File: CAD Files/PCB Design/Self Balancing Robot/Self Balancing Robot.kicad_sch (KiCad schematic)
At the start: 9 parts, among them M1 Stepper_Motor_bipolar, M2 Stepper_Motor_bipolar, U1 DEVKIT_V1_ESP32-WROOM-32, U2 TSR_1-2450

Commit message: Added battery terminal, updated capacitor symbol, and assigned footprints.
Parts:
- removed C1, C2: 100 μF, symbol Device:C
- removed U1: DEVKIT_V1_ESP32-WROOM-32, DEVKIT_V1_ESP32-WROOM-32:MODULE_DEVKIT_V1_ESP32-WROOM-32, symbol DEVKIT_V1_ESP32-WROOM-32:DEVKIT_V1_ESP32-WROOM-32
- added C1, C2: ECA1HM101, TW Footprints:CAPPRD350W60D800H1150, symbol TW_Symbols:ECA1HM101
- added J1: Screw_Terminal_01x02, TerminalBlock:TerminalBlock_MaiXu_MX126-5.0-02P_1x02_P5.00mm, symbol Connector:Screw_Terminal_01x02
- added U1: DEVKIT_V1_ESP32-WROOM-32, TW Footprints:MODULE_DEVKIT_V1_ESP32-WROOM-32, symbol TW_Symbols:DEVKIT_V1_ESP32-WROOM-32
- M1, M2: footprint (none) -> Connector_JST:JST_XH_B4B-XH-A_1x04_P2.50mm_Vertical
- MPU1: footprint (none) -> Connector_PinHeader_1.00mm:PinHeader_1x08_P1.00mm_Vertical
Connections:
- net +12V: now also C1.P, C2.P, J1.1 (Pin_1)
- net Direc1: now also U1.10 (D19)
- net Direc2: now also U1.24 (D26)
- net GND: now also C1.N, C2.N, J1.2 (Pin_2), U1.2 (GND), U1.29 (GND)
- net SCL: now also U1.14 (D22)
- net SDA: now also U1.11 (D21)
- net Step1: now also U1.9 (D18)
- net Step2: now also U1.23 (D25)
- net VDD: now also A2.13 (~{RESET}), A2.14 (~{SLEEP}), U1.30 (VIN)

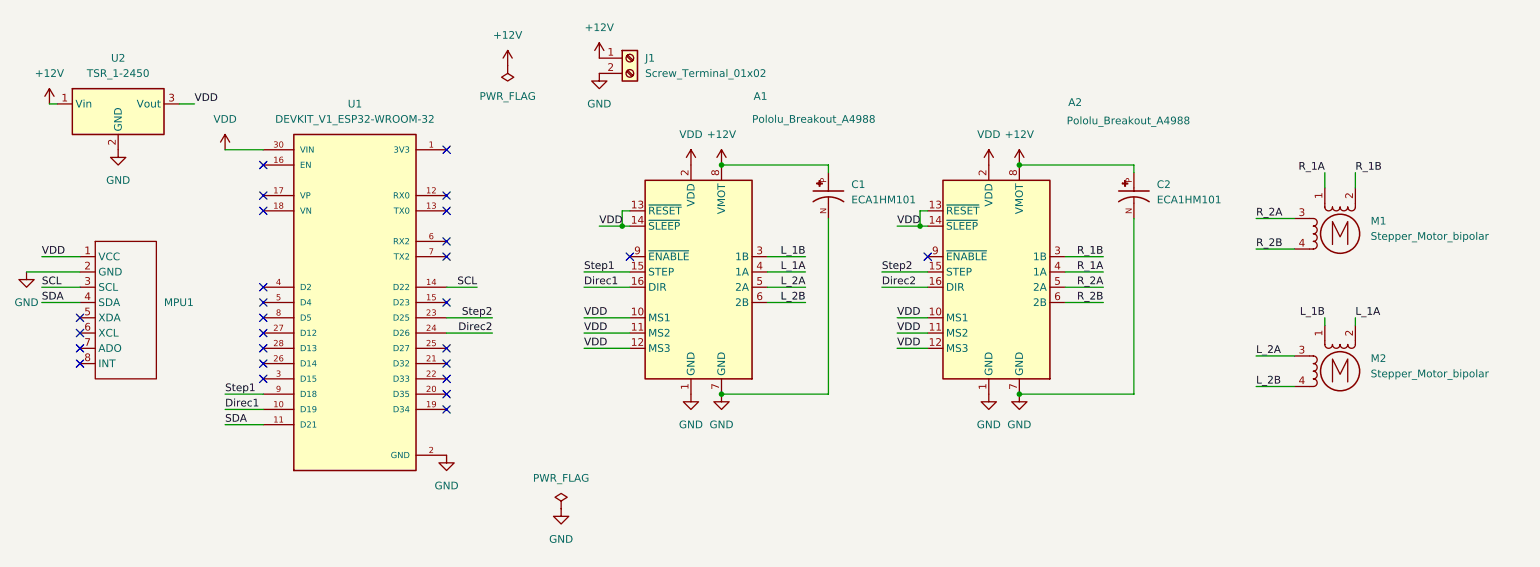
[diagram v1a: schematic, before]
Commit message: Fix schematic by adding screw terminal for battery, added indicator LEDS (and resistors), made custom footprints for capacitors, LEDS, configured libraries, made gitignore for PCB design folder
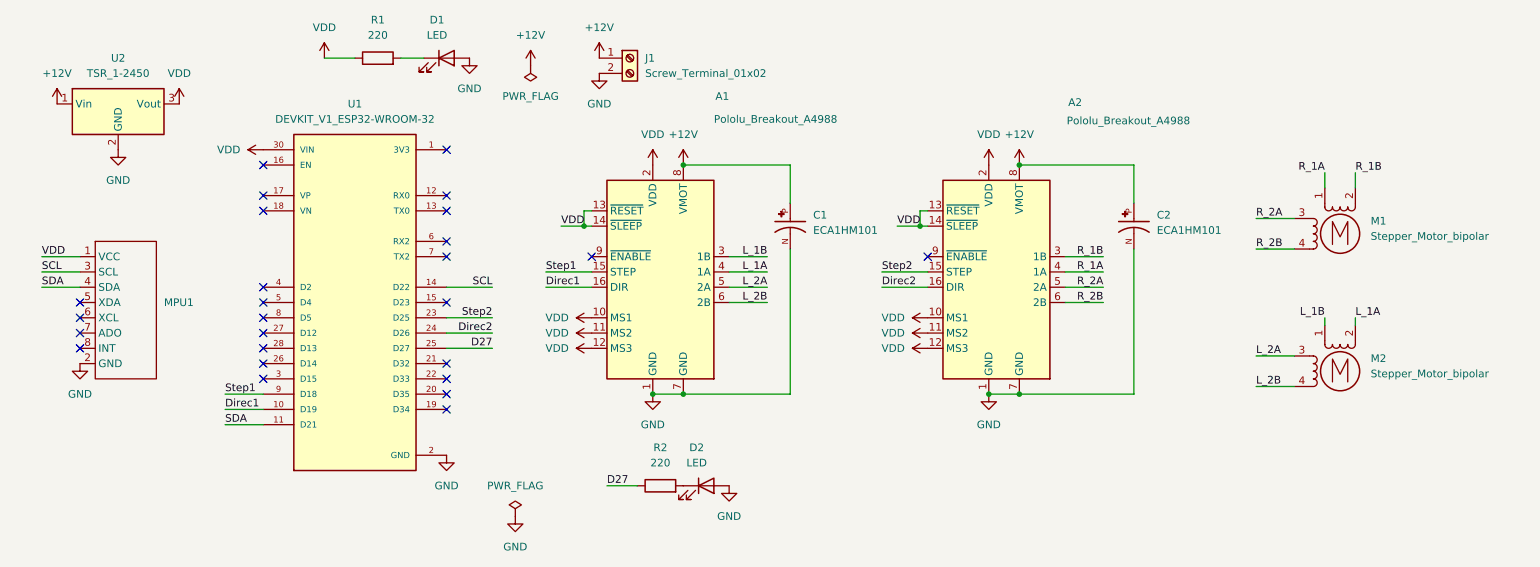
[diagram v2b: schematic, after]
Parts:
- added D1, D2: LED, TW Footprints:SMD LED 1206, symbol Device:LED
- added R1, R2: 220, Resistor_SMD:R_1206_3216Metric_Pad1.30x1.75mm_HandSolder, symbol Device:R
- C1, C2: footprint TW Footprints:CAPPRD350W60D800H1150 -> TW Footprints:CP_Radial_D6.3mm_P2.50mm
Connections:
- net GND: now also D1.2 (A), D2.2 (A)
- net VDD: now also R1.1
- net D27: now reaches U1.25 (D27)
- net D27: now also R2.1
- new net: D2.1 (K), R2.2
- new net: D1.1 (K), R1.2
- no-connect marks 27 -> 26
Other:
- moved on the sheet: A1, C1, C2

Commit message: Added MPU (GY-521) footprint
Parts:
- MPU1: footprint Connector_PinHeader_1.00mm:PinHeader_1x08_P1.00mm_Vertical -> TW Footprints:MODULE_GY-521
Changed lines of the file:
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@@
 			)
 		)
-		(property "Footprint" "Connector_PinHeader_1.00mm:PinHeader_1x08_P1.00mm_Vertical"
+		(property "Footprint" "TW Footprints:MODULE_GY-521"
 			(at 44.45 58.42 0)
 			(effects

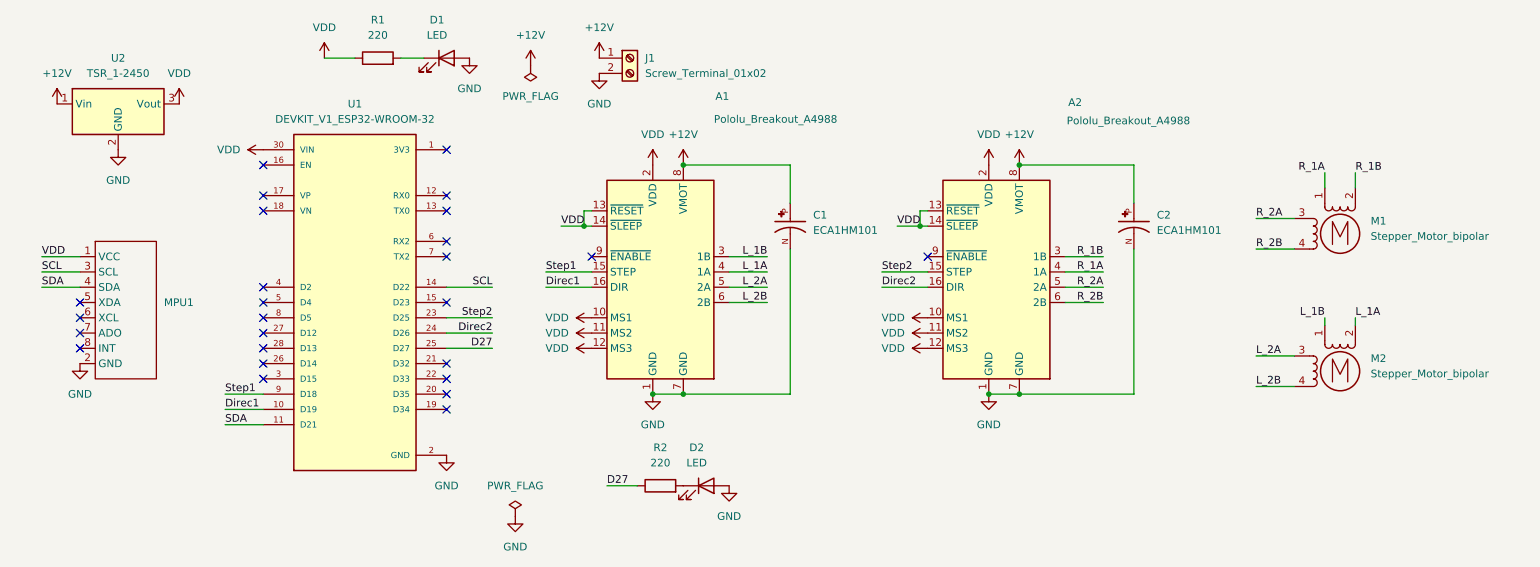
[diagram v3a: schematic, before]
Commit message: Positioned components on PCB, drew traces, assigned step files
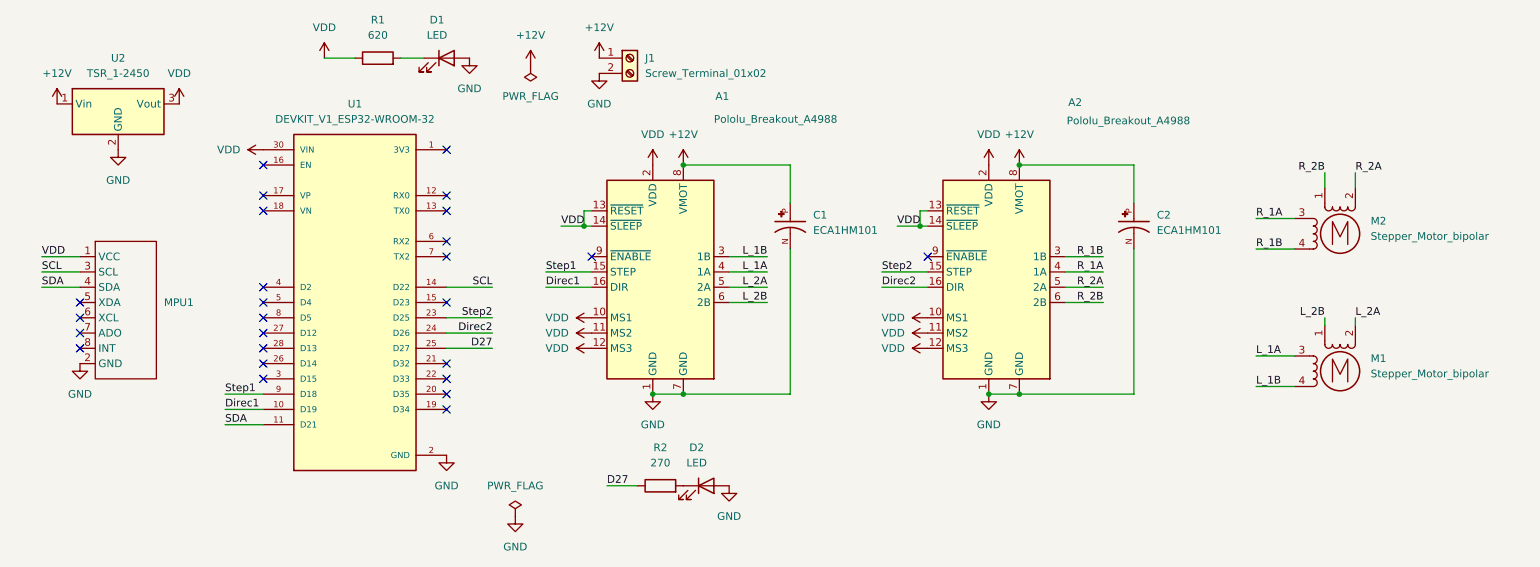
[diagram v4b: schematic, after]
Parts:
- M1: renamed from M2; footprint Connector_JST:JST_XH_B4B-XH-A_1x04_P2.50mm_Vertical -> Connector_JST:JST_EH_S4B-EH_1x04_P2.50mm_Horizontal
- M2: renamed from M1; footprint Connector_JST:JST_XH_B4B-XH-A_1x04_P2.50mm_Vertical -> Connector_JST:JST_EH_S4B-EH_1x04_P2.50mm_Horizontal
- R1: value 220 -> 620
- R2: value 220 -> 270
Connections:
- net L_1A: now also M1.3; no longer M1.2 (-)
- net L_1B: now also M1.4; no longer M1.1
- net L_2A: now also M1.2 (-); no longer M1.3
- net L_2B: now also M1.1; no longer M1.4
- net R_1A: now also M2.3; no longer M2.1
- net R_1B: now also M2.4; no longer M2.2 (-)
- net R_2A: now also M2.2 (-); no longer M2.3
- net R_2B: now also M2.1; no longer M2.4
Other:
- title: Self Bancing Robot -> Training Wheels Schematic
